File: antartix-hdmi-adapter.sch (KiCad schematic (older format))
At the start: 16 parts, among them IC2 TPD8S009DSMR, IC3 TPD8S009DSMR, J7 QTE-020-04-L-D-A, J8 685119134923

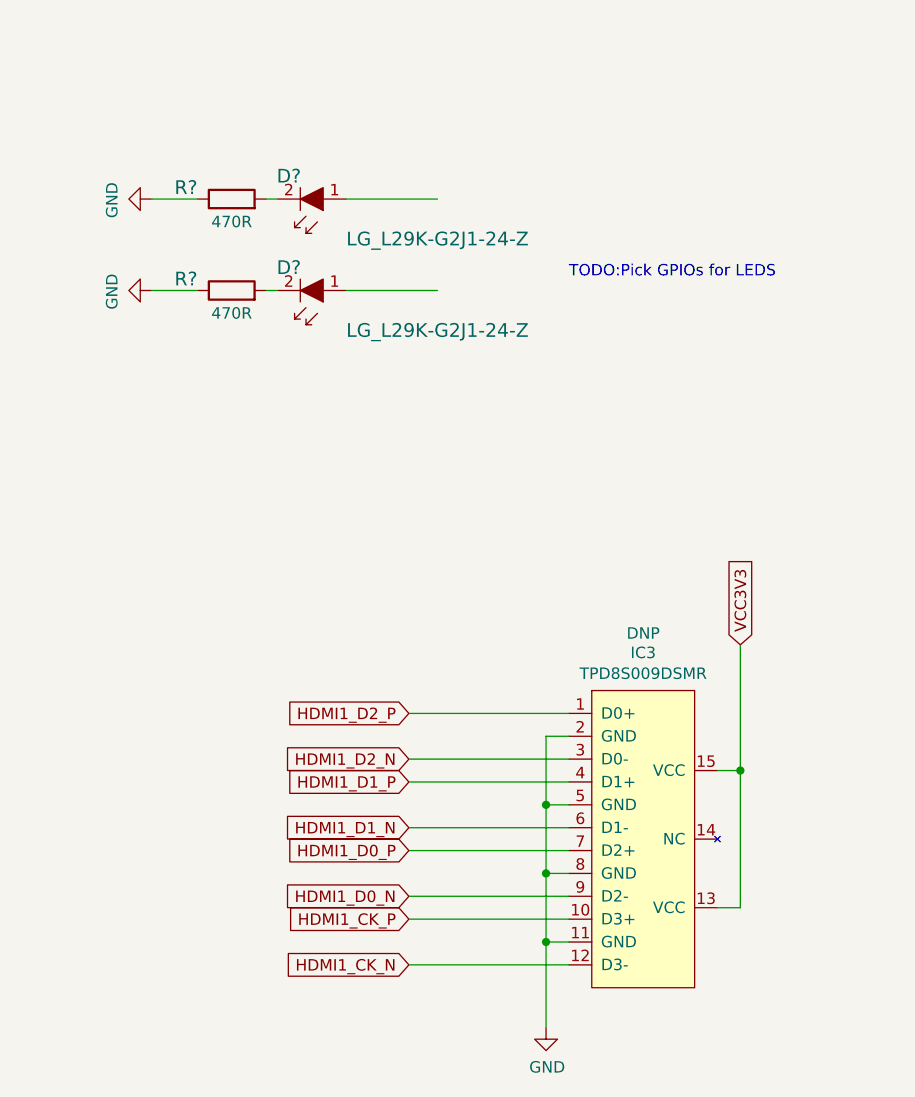
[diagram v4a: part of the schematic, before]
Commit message: Add component placement
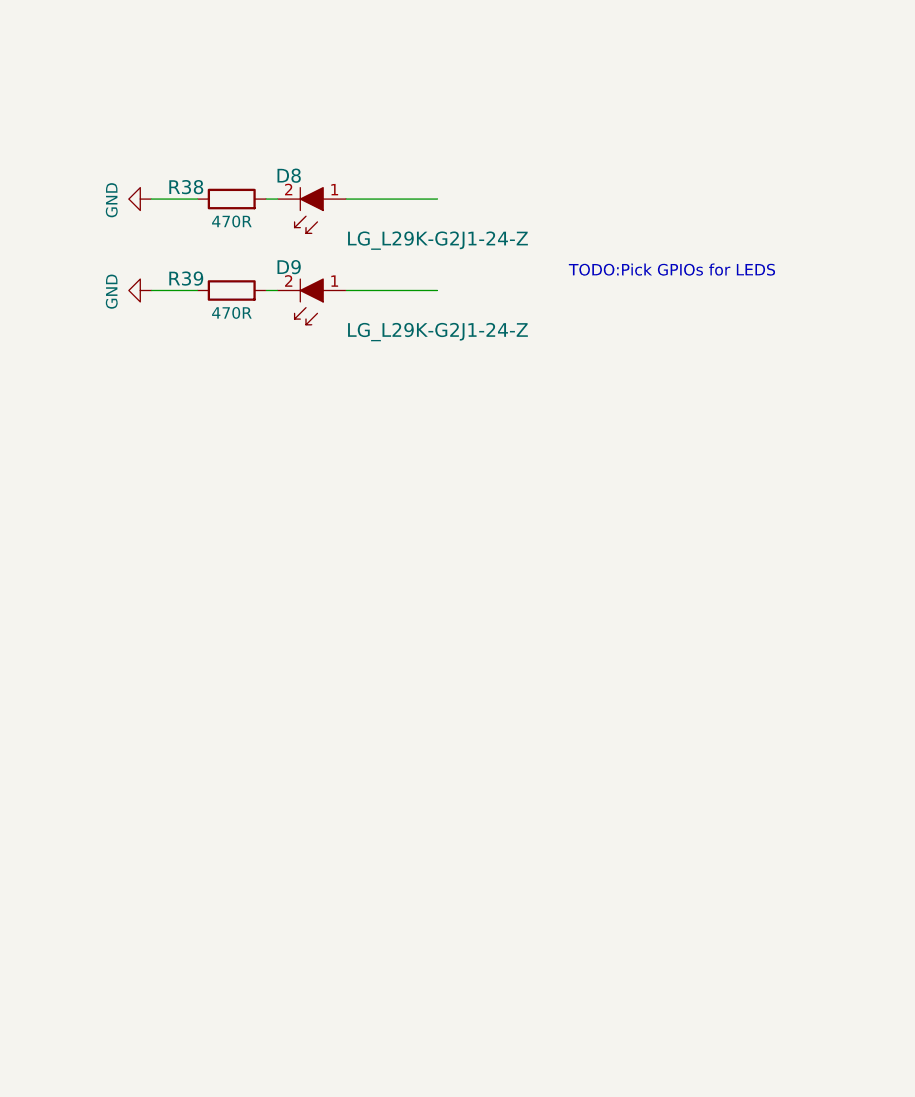
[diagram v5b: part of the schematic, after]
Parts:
- removed IC3: TPD8S009DSMR, antmicro-footprints:R-PDSO-N15, symbol antmicroTVSDiodes:TPD8S009DSMR
- gave numbers to parts that had none: 4
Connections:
- wire segments 127 -> 107
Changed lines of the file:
@@
-	1    0    0    -1
-$EndComp
-$Comp
-L antmicroTVSDiodes:TPD8S009DSMR IC3
-U 1 1 604E9D00
-P 11425 4825
-AR Path="/604C47E1/604E9D00" Ref="IC3"  Part="1"
-AR Path="/60603DE8/604E9D00" Ref="IC?"  Part="1"
-F 0 "IC3" H 11450 5340 50  0000 C CNN
-F 1 "TPD8S009DSMR" H 11450 5249 50  0000 C CNN
-F 2 "antmicro-footprints:R-PDSO-N15" H 12825 4475 50  0001 C CNN
-F 3 "" H 13125 4375 50  0001 C CNN
-F 4 "TPD8S009DSMR" H 11375 5325 50  0001 C CNN "MPN"
-F 5 "Texas Instruments" H 11475 5425 50  0001 C CNN "Manufacturer"
-F 6 "DNP" H 11450 5425 50  0000 C CNN "Populate"
-	1    11425 4825
-	1    0    0    -1
-$EndComp
-Wire Wire Line
-	11125 4675 11025 4675
-Wire Wire Line
-	11025 5575 11125 5575
-Wire Wire Line
-	11025 4675 11025 4975
-Connection ~ 11025 5575
-Wire Wire Line
-	11025 5575 11025 5950
-Wire Wire Line
-	11125 5275 11025 5275
-Connection ~ 11025 5275
-Wire Wire Line
-	11025 5275 11025 5575
-Wire Wire Line
-	11125 4975 11025 4975
-Connection ~ 11025 4975
-Wire Wire Line
-	11025 4975 11025 5275
-Wire Wire Line
-	11775 5425 11875 5425
-Wire Wire Line
-	11875 4825 11775 4825
-Wire Wire Line
-	11875 4275 11875 4825
-Connection ~ 11875 4825
-Wire Wire Line
-	11875 4825 11875 5425
-Text GLabel 11875 4275 1    50   Input ~ 0
-VCC3V3
-Wire Wire Line
-	11125 4575 10425 4575
-Wire Wire Line
-	11125 4775 10425 4775
-Wire Wire Line
-	11125 4875 10425 4875
-Wire Wire Line
-	11125 5075 10425 5075
-Wire Wire Line
-	11125 5175 10425 5175
-Wire Wire Line
-	11125 5375 10425 5375
-Wire Wire Line
-	11125 5475 10425 5475
-Wire Wire Line
-	11125 5675 10425 5675
-Text GLabel 10425 5475 0    50   Input ~ 0
-HDMI1_CK_P
-Text GLabel 10425 5675 0    50   Input ~ 0
-HDMI1_CK_N
-Text GLabel 10425 5175 0    50   Input ~ 0
-HDMI1_D0_P
-Text GLabel 10425 5375 0    50   Input ~ 0
-HDMI1_D0_N
-Text GLabel 10425 4875 0    50   Input ~ 0
-HDMI1_D1_P
-Text GLabel 10425 5075 0    50   Input ~ 0
-HDMI1_D1_N
-Text GLabel 10425 4775 0    50   Input ~ 0
-HDMI1_D2_N
-Text GLabel 10425 4575 0    50   Input ~ 0
-HDMI1_D2_P
-$Comp
-L power:GND #PWR076
-U 1 1 604E9D47
-P 11025 5950
-AR Path="/604C47E1/604E9D47" Ref="#PWR076"  Part="1"
-AR Path="/60603DE8/604E9D47" Ref="#PWR?"  Part="1"
-F 0 "#PWR076" H 11025 5700 50  0001 C CNN
-F 1 "GND" H 11030 5777 50  0000 C CNN
-F 2 "" H 11025 5950 50  0001 C CNN
-F 3 "" H 11025 5950 50  0001 C CNN
-	1    11025 5950
 	1    0    0    -1
 $EndComp
@@
 AR Path="/616A7868" Ref="R?"  Part="1"
 AR Path="/60924187/616A7868" Ref="R?"  Part="1"
-F 0 "R?" H 9450 2775 60  0000 C CNN
+AR Path="/604C47E1/616A7868" Ref="R39"  Part="1"
+F 0 "R39" H 9450 2775 60  0000 C CNN
 F 1 "R_470R_0402" H 9650 2575 60  0001 C CNN
 F 2 "antartix-arty-controller-footprints:0402-res" H 9850 2925 60  0001 L CNN
@@
 AR Path="/616A786E" Ref="#PWR?"  Part="1"
 AR Path="/60924187/616A786E" Ref="#PWR?"  Part="1"
-F 0 "#PWR?" H 9300 2475 50  0001 C CNN
+AR Path="/604C47E1/616A786E" Ref="#PWR0101"  Part="1"
+F 0 "#PWR0101" H 9300 2475 50  0001 C CNN
 F 1 "GND" H 9305 2552 50  0000 C CNN
 F 2 "" H 9300 2725 50  0001 C CNN
@@
 AR Path="/616A7878" Ref="D?"  Part="1"
 AR Path="/60924187/616A7878" Ref="D?"  Part="1"
-F 0 "D?" H 10000 2625 60  0000 C CNN
+AR Path="/604C47E1/616A7878" Ref="D9"  Part="1"
+F 0 "D9" H 10000 2625 60  0000 C CNN
 F 1 "LG_L29K-G2J1-24-Z" H 9350 2900 60  0000 C CNN
 F 2 "antartix-arty-controller-footprints:LED_0603" H 10150 2925 60  0001 L CNN
@@
 AR Path="/616A7883" Ref="R?"  Part="1"
 AR Path="/60924187/616A7883" Ref="R?"  Part="1"
-F 0 "R?" H 9450 2375 60  0000 C CNN
+AR Path="/604C47E1/616A7883" Ref="R38"  Part="1"
+F 0 "R38" H 9450 2375 60  0000 C CNN
 F 1 "R_470R_0402" H 9650 2175 60  0001 C CNN
 F 2 "antartix-arty-controller-footprints:0402-res" H 9850 2525 60  0001 L CNN
@@
 AR Path="/616A7889" Ref="#PWR?"  Part="1"
 AR Path="/60924187/616A7889" Ref="#PWR?"  Part="1"
-F 0 "#PWR?" H 9300 2075 50  0001 C CNN
+AR Path="/604C47E1/616A7889" Ref="#PWR0102"  Part="1"
+F 0 "#PWR0102" H 9300 2075 50  0001 C CNN
 F 1 "GND" H 9305 2152 50  0000 C CNN
 F 2 "" H 9300 2325 50  0001 C CNN
@@
 AR Path="/616A7894" Ref="D?"  Part="1"
 AR Path="/60924187/616A7894" Ref="D?"  Part="1"
-F 0 "D?" H 10000 2225 60  0000 C CNN
+AR Path="/604C47E1/616A7894" Ref="D8"  Part="1"
+F 0 "D8" H 10000 2225 60  0000 C CNN
 F 1 "LG_L29K-G2J1-24-Z" H 9350 2500 60  0000 C CNN
 F 2 "antartix-arty-controller-footprints:LED_0603" H 10150 2525 60  0001 L CNN

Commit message: Add FTDI and LEDs
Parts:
- added C? (x2): C_100n_0402, antartix-arty-controller-footprints:0402-cap, symbol antartix-arty-controller:C_100n_0402
- added C?: C_1u_0402, antmicro-footprints:0402-cap, symbol antmicroCapacitors0402:C_1u_0402
- added D?: TPD2E009, antartix-arty-controller-footprints:SOT-3, symbol antartix-arty-controller:TPD2E009
- added J?: WE_629105150521, antartix-arty-controller-footprints:USB_Micro_B_Female_629105150521, symbol antartix-arty-controller:WE_629105150521
- added R?: R_4k7_0402, antartix-arty-controller-footprints:0402-res, symbol antartix-arty-controller:R_4k7_0402
- added R?: R_10k_0402, antartix-arty-controller-footprints:0402-res, symbol antartix-arty-controller:R_10k_0402
- added R? (x2): R_0R_0805, antmicro-footprints:0805-res, symbol antmicroResistorsmisc:R_0R_0805
- added U?: FT230XS-R, antmicro-footprints:SOIC-16_W3.90mm, symbol antmicroInterfaceControllers:FT230XS-R
- R37: DNP (none) -> DNP; Populate DNP -> (none)
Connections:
- net labels added: LED0, LED1, USB_CON_N, USB_CON_P, VCC5V0
- wire segments 107 -> 147
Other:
- note added: "Micro USB - RPiCM console"
- note added: "USE mini/micro HDMI"
- note removed: "TODO:Pick GPIOs for LEDS"

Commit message: Add HDMI control signals, change connector to mini HDMI
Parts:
- removed J8: 685119134923, antmicro-footprints:HDMI_A_Female_685119134923, symbol antmicroUSBDVIHDMIConnectors:685119134923
- removed TP1, TP2, TP3, TP4, TP5: TP_SMD1MM, antmicro-footprints:Testpoint_smd_1mm, symbol antmicroTestPoints:TP_SMD1MM
- added C?: C_100n_0402, antartix-arty-controller-footprints:0402-cap, symbol antartix-arty-controller:C_100n_0402
- added C?: C_1u_0402, antmicro-footprints:0402-cap, symbol antmicroCapacitors0402:C_1u_0402
- added C?: C_22u_0603, antmicro-footprints:0603-cap, symbol antmicroCapacitors0603:C_22u_0603
- added FB?: BLM21SP111BH1, antartix-arty-controller-footprints:0805-res, symbol antartix-arty-controller:BLM21SP111BH1
- added J?: WE_685119136923, antmicro-footprints:WE_685119136923, symbol antmicroUSBDVIHDMIConnectors:WE_685119136923
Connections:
- wire segments 147 -> 153
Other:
- note removed: "USE mini/micro HDMI"
- moved on the sheet: D8, D9, IC2, R38, R39

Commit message: Fix power keys
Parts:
- added C? (x3): C_470p_0402, antmicro-footprints:0402-cap, symbol antmicroCapacitors0402:C_470p_0402
- added J?: Screw_Terminal_01x08, Connector_Phoenix_MC:PhoenixContact_MCV_1,5_8-G-3.5_1x08_P3.50mm_Vertical, symbol Connector:Screw_Terminal_01x08
- added Q? (x3): FDC6330L, antmicro-footprints:FDC6330L, symbol antmicroPMICPowerDistributionSwitchesLoadDrivers:FDC6330L
- added R? (x3): R_1k_0402, antmicro-footprints:0402-res, symbol antmicroResistors0402:R_1k_0402
- added R? (x3): R_47k_0402, antartix-arty-controller-footprints:0402-res, symbol antartix-arty-controller:R_47k_0402
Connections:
- net labels added: GND1, GND2, GND3, GND_IN, USB1_EN, USB2_EN, USB3_EN, VCC_9V_IN, VCC_9V_OUT_1, VCC_9V_OUT_2, VCC_9V_OUT_3
- wire segments 153 -> 206
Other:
- note added: "TODO:Replace with 3-794680-8 + 794617-8 + 1-794610-1"
- note added: "TODO:Replace with MC 1,5/ 8-G-3,5 + MCVW 1,5/8-ST-3,5"
- note added: "TODO:Replace with some small pitch terminal"
